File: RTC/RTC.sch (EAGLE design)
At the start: 8 parts, among them IC1 DS3231/SO

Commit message: Latest version of schematics and boards
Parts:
- removed IC1: DS3231/SO, adafruit:DS3231/SO
- removed LED: blue, led:LEDCHIPLED_1206
- removed U$3: TINY841, IntegerLabs:TINY841
- added BAT1: 20mm coincell, SparkFun-Electromechanical:BATTERY20MM_4LEGS
- added C3: (no value), SparkFun-Capacitors:CAP0805
- added C4: .47uF, SparkFun-Capacitors:CAP0805
- added L1: 1mH, SparkFun-Passives:INDUCTOR1007
- added LED1: (no value), adafruit:LEDCHIP-LED0805
- added Q2: MC-405, crystal:MC-405
- added R1: 680, SparkFun-Passives:RESISTOR0805-RES
- added R2: 10k, SparkFun-Passives:RESISTOR0805-RES
- added R4: 1, SparkFun-Resistors:RESISTOR0805-RES
- added R5, R6: 2k, SparkFun-Resistors:RESISTOR0805-RES
- added T1: therm, SparkFun-Passives:RESISTOR0805-RES
- added U$1: ATTINY48/88-TQFP, IntegerLabs:ATTINY48/88-TQFP
- C1: value 0.1uF -> .47uF
- C2: value 10uF -> 2.2uF; device SparkFun-Capacitors:CAP0805 -> SparkFun-Passives:CAP0805
- R3: value 680 -> 1k
- U$2: value BATTERY -> PCF8523; device IntegerLabs:BATTERY -> IntegerLabs:PCF8523
- U$4: value FOOTPRINT -> FOOTPRINTFOOTPRINT-2; device IntegerLabs:FOOTPRINT -> IntegerLabs:FOOTPRINTFOOTPRINT-2
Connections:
- removed net DATA: U$3.PA2
- removed net SCL/SCK: U$3.PA4, U$4.SCL
- removed net SDA/MOSI: U$3.PA6, U$4.SDA
- new net AVCC: C4.2, L1.1, R2.1, U$1.AVCC
- new net MOSI: U$1.PB3, U$4.MOSI
- new net N$7: Q2.1, U$2.OSCI
- new net N$8: Q2.2, U$2.OSCO
- new net RTC_CLKOUT: U$2.CLKOUT
- new net RTC_SCL: R5.1, U$1.PD2, U$2.SCL
- new net RTC_SDA: R6.1, U$1.PD1, U$2.SDA
- new net SCK: U$1.PB5, U$4.SCK
- new net SCL: U$1.PC5, U$4.SCL
- new net SDA: U$1.PC4, U$4.SDA
- new net THERM: C3.1, R2.2, T1.2, U$1.PC2
- net GND: now also BAT1.-, C2.2, C3.2, C4.1, LED1.C, T1.1, U$1.GND, U$1.GND@1, U$2.VSS; no longer C2.1, IC1.GND, LED.C, U$2.-, U$3.GND
- net LED: now also R1.2, U$1.PB1; no longer R3.2, U$3.PA1
- net MISO: now also U$1.PB4; no longer U$3.PA5
- net N$2: now also R4.2, U$4.VCC; no longer IC1.SCL, U$3.PB0
- net N$3: now also C2.1, R3.1, U$2.VDD; no longer IC1.SDA, U$3.PB1
- net N$5: now also LED1.A, R1.1; no longer LED.A, R3.1
- net RESET: now also U$1.PC6; no longer U$3.PB3
- net VBAT: now also BAT1.+, U$2.VBAT; no longer IC1.VBAT, U$2.+
- net VCC: now also L1.2, R3.2, R4.1, R5.2, R6.2, U$1.VCC, U$4.VPROG; no longer C2.2, IC1.VCC, U$3.VCC, U$4.+5V
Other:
- moved on the sheet: C1, C2, R3

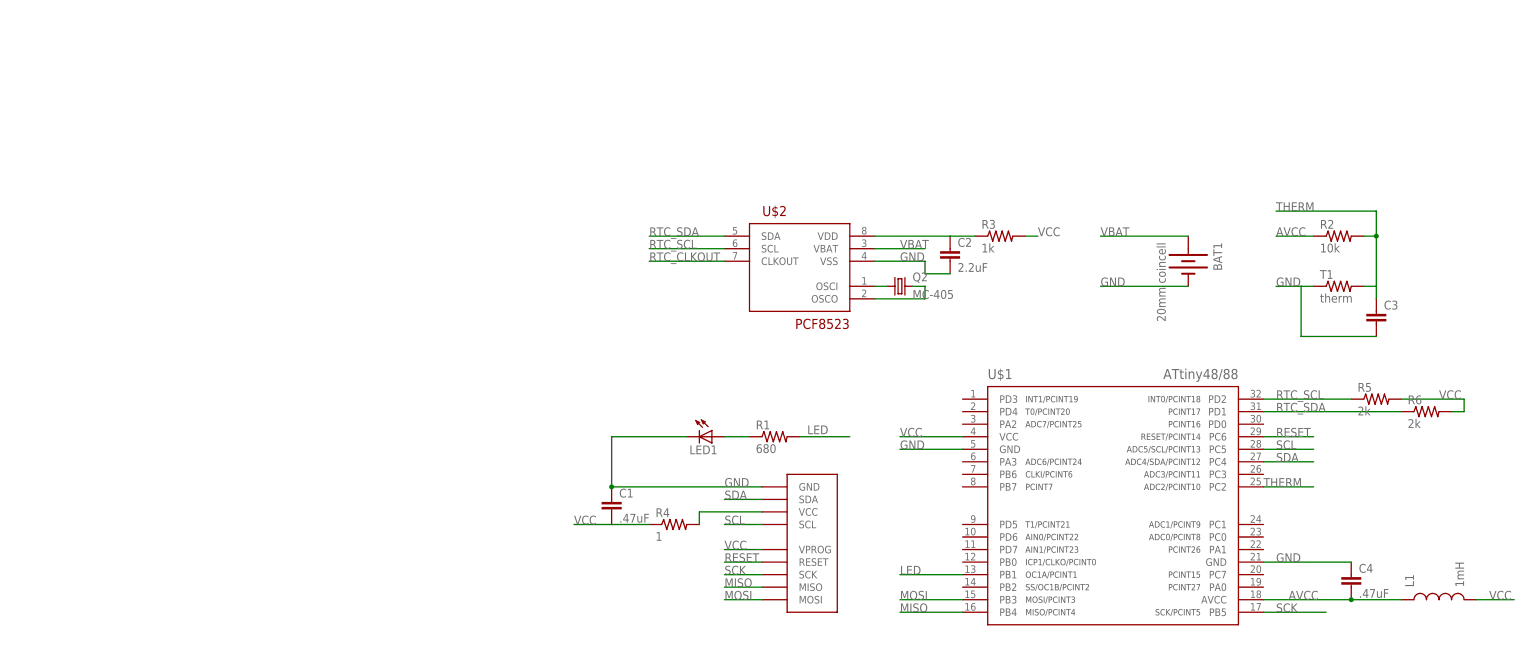
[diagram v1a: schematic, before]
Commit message: Changed to use attiny841
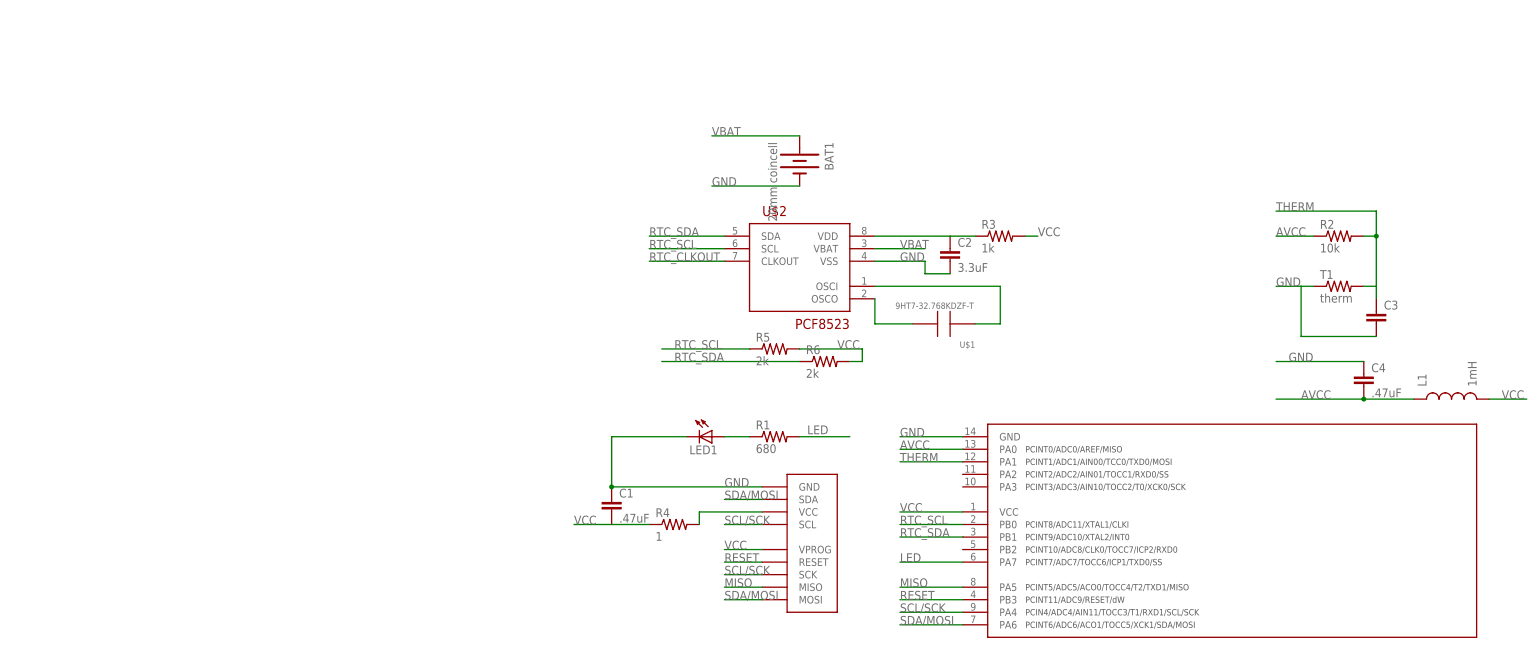
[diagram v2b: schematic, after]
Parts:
- removed Q2: MC-405, crystal:MC-405
- added U$3: TINY841, IntegerLabs:TINY841
- C2: value 2.2uF -> 3.3uF
- U$1: value ATTINY48/88-TQFP -> 9HT7-32.768KDZF-T; device IntegerLabs:ATTINY48/88-TQFP -> IntegerLabs:CRYSTALABS25
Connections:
- removed net MOSI: U$1.PB3, U$4.MOSI
- removed net N$7: Q2.1, U$2.OSCI
- removed net N$8: Q2.2, U$2.OSCO
- removed net SCK: U$1.PB5, U$4.SCK
- removed net SCL: U$1.PC5, U$4.SCL
- removed net SDA: U$1.PC4, U$4.SDA
- new net N$4: U$1.P$1, U$2.OSCI
- new net N$6: U$1.P$2, U$2.OSCO
- new net SCL/SCK: U$3.PA4, U$4.SCK, U$4.SCL
- new net SDA/MOSI: U$3.PA6, U$4.MOSI, U$4.SDA
- net AVCC: now also U$3.PA0; no longer U$1.AVCC
- net GND: now also U$3.GND; no longer U$1.GND, U$1.GND@1
- net LED: now also U$3.PA7; no longer U$1.PB1
- net MISO: now also U$3.PA5; no longer U$1.PB4
- net RESET: now also U$3.PB3; no longer U$1.PC6
- net RTC_SCL: now also U$3.PB0; no longer U$1.PD2
- net RTC_SDA: now also U$3.PB1; no longer U$1.PD1
- net THERM: now also U$3.PA1; no longer U$1.PC2
- net VCC: now also U$3.VCC; no longer U$1.VCC
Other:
- moved on the sheet: BAT1, C4, L1, R5, R6

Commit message: Switched to attiny841 and made the battery insert from the side.
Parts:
- C3: value (none) -> .1uF
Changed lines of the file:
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@@
 <part name="R2" library="SparkFun-Passives" deviceset="RESISTOR" device="0805-RES" value="10k"/>
 <part name="T1" library="SparkFun-Passives" deviceset="RESISTOR" device="0805-RES" value="therm"/>
-<part name="C3" library="SparkFun-Capacitors" deviceset="CAP" device="0805"/>
+<part name="C3" library="SparkFun-Capacitors" deviceset="CAP" device="0805" value=".1uF"/>
 <part name="BAT1" library="SparkFun-Electromechanical" deviceset="BATTERY" device="20MM_4LEGS" value="20mm coincell"/>
 <part name="U$2" library="IntegerLabs" deviceset="PCF8523" device=""/>

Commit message: Checkpointing PCB designs
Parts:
- C2: value 3.3uF -> 10uF
- U$4: BOARD (none) -> Clock; VERSION (none) -> v5
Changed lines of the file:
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@@
 <layers>
 <layer number="1" name="Top" color="4" fill="1" visible="no" active="no"/>
+<layer number="2" name="Route2" color="1" fill="3" visible="no" active="no"/>
+<layer number="3" name="Route3" color="4" fill="3" visible="no" active="no"/>
+<layer number="14" name="Route14" color="1" fill="6" visible="no" active="no"/>
+<layer number="15" name="Route15" color="4" fill="6" visible="no" active="no"/>
 <layer number="16" name="Bottom" color="1" fill="1" visible="no" active="no"/>
 <layer number="17" name="Pads" color="2" fill="1" visible="no" active="no"/>
@@
 <part name="C1" library="SparkFun-Capacitors" deviceset="CAP" device="0805" value=".47uF"/>
 <part name="R1" library="SparkFun-Passives" deviceset="RESISTOR" device="0805-RES" value="680"/>
-<part name="U$4" library="IntegerLabs" deviceset="FOOTPRINT" device="FOOTPRINT-2" value="FOOTPRINTFOOTPRINT-2"/>
+<part name="U$4" library="IntegerLabs" deviceset="FOOTPRINT" device="FOOTPRINT-2" value="FOOTPRINTFOOTPRINT-2">
+<attribute name="BOARD" value="Clock"/>
+<attribute name="VERSION" value="v5"/>
+</part>
 <part name="R2" library="SparkFun-Passives" deviceset="RESISTOR" device="0805-RES" value="10k"/>
 <part name="T1" library="SparkFun-Passives" deviceset="RESISTOR" device="0805-RES" value="therm"/>
@@
 <part name="LED1" library="adafruit" deviceset="LED" device="CHIP-LED0805"/>
 <part name="R3" library="SparkFun-Passives" deviceset="RESISTOR" device="0805-RES" value="1k"/>
-<part name="C2" library="SparkFun-Passives" deviceset="CAP" device="0805" value="3.3uF"/>
+<part name="C2" library="SparkFun-Passives" deviceset="CAP" device="0805" value="10uF"/>
 <part name="R5" library="SparkFun-Resistors" deviceset="RESISTOR" device="0805-RES" value="2k"/>
 <part name="R6" library="SparkFun-Resistors" deviceset="RESISTOR" device="0805-RES" value="2k"/>
